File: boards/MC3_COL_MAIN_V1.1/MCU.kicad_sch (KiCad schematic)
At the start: 52 parts, among them J2 SWD, SW1 SKRKAEE020, U10 GP1S094HCZ0F, U11 GP1S094HCZ0F, U2 STM32U595RJT6, U9 AEDR-8300-1Q0, Y1 8MHz

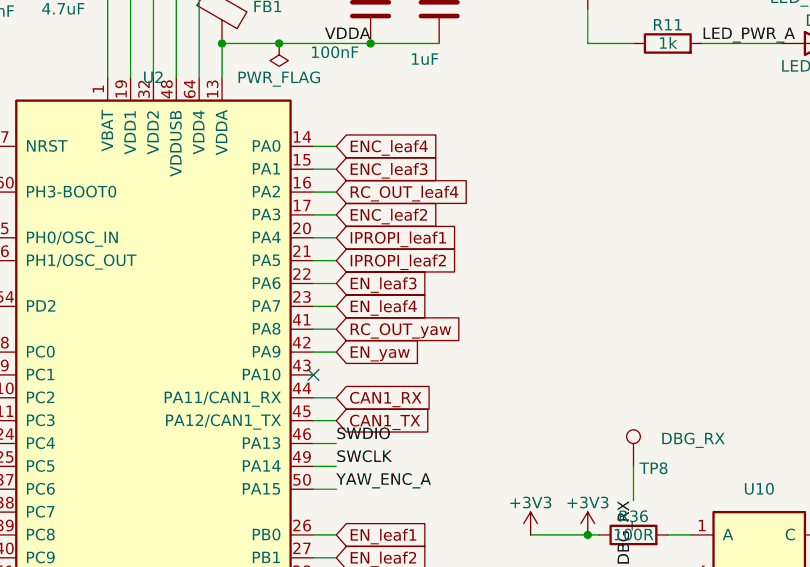
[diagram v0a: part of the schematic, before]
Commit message: V1.1 pre-order (replayed on refactored sheets): ENC_leaf2<->RC_OUT_leaf4 swapped PA3/PA2 (PA3 is TT, PP SENT unsafe); J14 fifth encoder FFC + R48 = YAW_ABS on PA10 (FT); ioc updated; ERC 0/0
Co-Authored-By: Claude Fable 5 <noreply@anthropic.com>
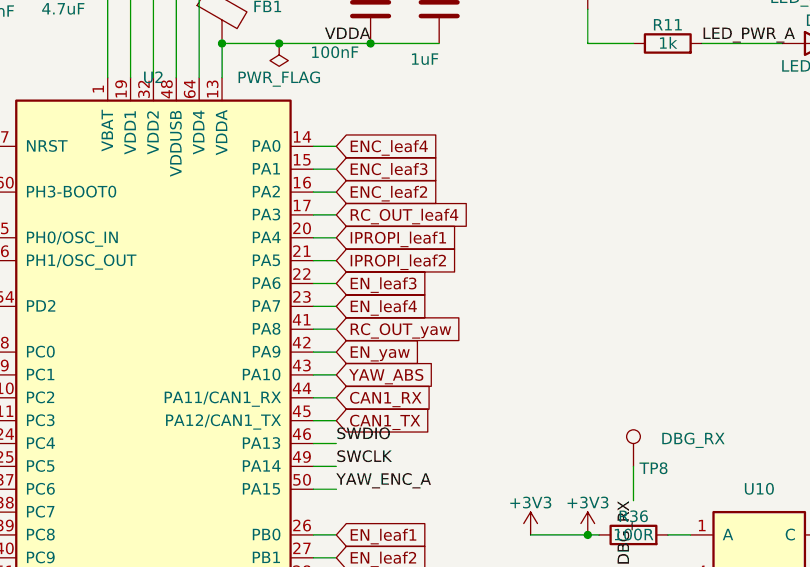
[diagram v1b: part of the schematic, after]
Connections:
- net ENC_leaf2: now also U2.16 (PA2); no longer U2.17 (PA3)
- net RC_OUT_leaf4: now also U2.17 (PA3); no longer U2.16 (PA2)
- net YAW_ABS: now reaches U2.43 (PA10)
- no-connect marks 4 -> 3
